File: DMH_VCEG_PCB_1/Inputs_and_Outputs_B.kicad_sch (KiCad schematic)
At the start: 38 parts, among them J11 TS_Jack_6.35mm_Sw, J12 TS_Jack_6.35mm_Sw, J13 TS_Jack_6.35mm_Sw, J14 TS_Jack_6.35mm_Sw, J15 TS_Jack_6.35mm_Sw, J16 TS_Jack_6.35mm_Sw, J17 TS_Jack_6.35mm_Sw, J18 TS_Jack_6.35mm_Sw, J19 TS_Jack_6.35mm_Sw, J20 TS_Jack_6.35mm_Sw, J24 Conn_01x10_PinHeader, J25 Conn_01x10_PinHeader, J26 Conn_01x10_PinHeader, J27 Conn_01x06_PinHeader, U18 TL074, U21 TL074

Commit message: Copied circuit A to B
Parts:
- added R15: 1k, Resistor_THT:R_Axial_DIN0207_L6.3mm_D2.5mm_P7.62mm_Horizontal, symbol Device:R_US
- added R22: 68K, Resistor_THT:R_Axial_DIN0207_L6.3mm_D2.5mm_P7.62mm_Horizontal, symbol Device:R_US
- added R24: 100k, Resistor_THT:R_Axial_DIN0207_L6.3mm_D2.5mm_P7.62mm_Horizontal, symbol Device:R_US
- added U18: TL074, Package_DIP:DIP-14_W7.62mm_Socket, symbol Amplifier_Operational:TL074
- renumbered J24 to J22, R114 to R16, R78 to R17, R73 to R18, R74 to R19, R75 to R20, R76 to R21, R148 to R23, R77 to R25, R56 to R26, R147 to R27, R79 to R28, RV23 to RV12, RV24 to RV13, RV25 to RV14, RV26 to RV15, RV51 to RV16, RV27 to RV17, RV28 to RV18, RV29 to RV19, RV30 to RV20, RV50 to RV21, RV49 to RV22, U21 to U11, U18 to U22
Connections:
- net GND: now also U18.10 (+)
- net SG Out B: now also R24.1; no longer J17.T
- new net: R22.1, R24.2, U18.9 (-)
- new net: R15.2, R22.2, U18.8
- new net: J17.T, R15.1

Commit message: Divided components between PCB 1 and 2
Still need to:
- Place interface pins where needed
- Set "exclude from board" options where needed
- Copy schematic over to PCB 2 project
- Invert "exclude from board" options where needed
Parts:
- removed J27: Conn_01x06_PinHeader, symbol SynthStuff:Conn_01x06_PinHeader
- renumbered J22 to J?, U11 to U17
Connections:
- net GND: now also U18.12 (+); no longer U18.10 (+)
- net at R22.1, R24.2: now also U18.13 (-); no longer U18.9 (-)
- net at R15.2, R22.2: now also U18.14; no longer U18.8
- net at R17.1, RV16.1: now also U17.5 (+); no longer U17.12 (+)
- net at R27.1, RV21.1: now also U17.3 (+); no longer U17.10 (+)
- net at R25.1, R26.1, RV22.1: now also U17.1; no longer U17.8
- net at R28.2, RV22.2, RV22.3: now also U17.2 (-); no longer U17.9 (-)
- net at R23.1, R26.2: now also U17.6 (-); no longer U17.13 (-)
- net at R16.1, R23.2: now also U17.7; no longer U17.14

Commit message: Re-annotated whole circuit
Now need to place interface pins and determine in and out of board settings
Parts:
- gave numbers to parts that had none: 3
- renumbered J24 to J25, J25 to J26, R18 to R181, R19 to R182, R20 to R183, R21 to R184, R22 to R185, R24 to R186, R15 to R187, R25 to R188, R23 to R189, R28 to R190, R26 to R191, R16 to R192, R27 to R193, R17 to R194, RV17 to RV32, RV12 to RV33, RV18 to RV34, RV13 to RV35, RV19 to RV36, RV14 to RV37, RV20 to RV38, RV15 to RV39, RV22 to RV40, RV21 to RV41, RV16 to RV42, U22 to U23

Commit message: Ready for breadboarding
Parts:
- removed unit 1 of J24
- removed unit 2 of J25
- added J24: Conn_01x06_PinHeader, Connector_PinHeader_2.54mm:PinHeader_1x06_P2.54mm_Vertical, symbol SynthStuff:Conn_01x06_PinHeader
- added unit 10 of J25
- added unit 3 of J26
- added unit 2 of J27
- added unit 1 of J27
- RV40, RV41, RV42: footprint Potentiometer_THT:Potentiometer_Bourns_3296X_Horizontal -> Potentiometer_THT:Potentiometer_Bourns_3296W_Vertical
- U17: footprint (none) -> Package_DIP:DIP-14_W7.62mm_Socket
- renumbered J24 to J27, J22 to J27, J23 to J27
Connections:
- net +12V: now also J25.1 (Pin_1)
- net -12V: now also J27.2 (Pin_2); no longer J25.1 (Pin_1)
- net GND: now also J24.6 (Pin_6), J25.10 (Pin_10), J27.1 (Pin_1); no longer J26.2 (Pin_2)
- net SG Out B: now also J26.2 (Pin_2)
- net at J17.T, R187.1: now also J26.3 (Pin_3)

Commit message: PCB 2 placement in progress
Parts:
- RV32: Function Att CV B Zero Adj -> Att CV B Zero
- RV34: Function Dec CV B Zero Adj -> Dec CV B Zero
- RV36: Function Sus CV B Zero Adj -> Sus CV B Zero
- RV38: Function Rel CV B Zero Adj -> Rel CV B Zero
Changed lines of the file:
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@@
 			)
 		)
-		(property "Function" "Sus CV B Zero Adj"
+		(property "Function" "Sus CV B Zero"
 			(at 127 86.868 90)
 			(effects
@@
 			)
 		)
-		(property "Function" "Dec CV B Zero Adj"
+		(property "Function" "Dec CV B Zero"
 			(at 127 55.118 90)
 			(effects
@@
 			)
 		)
-		(property "Function" "Rel CV B Zero Adj"
+		(property "Function" "Rel CV B Zero"
 			(at 127 118.618 90)
 			(effects
@@
 			)
 		)
-		(property "Function" "Att CV B Zero Adj"
+		(property "Function" "Att CV B Zero"
 			(at 127 23.368 90)
 			(effects

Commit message: Synced changes to Circuit B
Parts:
- added R11: 100k, Resistor_THT:R_Axial_DIN0207_L6.3mm_D2.5mm_P7.62mm_Horizontal, symbol Device:R_US
- added R18: 68k, Resistor_THT:R_Axial_DIN0207_L6.3mm_D2.5mm_P7.62mm_Horizontal, symbol Device:R_US
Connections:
- net +12V: now also R18.1
- net GND: now also R11.2; no longer U18.12 (+)
- new net: R11.1, R18.2, U18.12 (+)
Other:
- moved on the sheet: R185, R187, U18D

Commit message: PCB 2 routing in progress
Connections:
- net Att CV B: no longer J27.3 (Pin_3)
- net Dec CV B: no longer J27.6 (Pin_6)
- net Rel CV B: no longer J27.10 (Pin_10)
- net Sus CV B: no longer J27.7 (Pin_7)
- no-connect marks 0 -> 4
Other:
- moved on the sheet: J27C, J27F, J27G, J27J
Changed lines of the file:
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@@
 	)
 	(junction
-		(at 144.78 129.54)
-		(diameter 0)
-		(color 0 0 0 0)
-	)
-	(junction
 		(at 176.53 215.9)
 		(diameter 0)
@@
 	)
 	(junction
-		(at 144.78 66.04)
-		(diameter 0)
-		(color 0 0 0 0)
-	)
-	(junction
-		(at 144.78 34.29)
-		(diameter 0)
-		(color 0 0 0 0)
-	)
-	(junction
 		(at 115.57 63.5)
 		(diameter 0)
@@
 	)
 	(junction
-		(at 144.78 97.79)
-		(diameter 0)
-		(color 0 0 0 0)
-	)
-	(junction
 		(at 138.43 85.09)
 		(diameter 0)
@@
 		(color 0 0 0 0)
 	)
+	(no_connect
+		(at 144.78 63.5)
+	)
+	(no_connect
+		(at 144.78 127)
+	)
+	(no_connect
+		(at 144.78 95.25)
+	)
+	(no_connect
+		(at 144.78 31.75)
+	)
 	(wire
 		(pts
@@
 	(wire
 		(pts
-			(xy 144.78 97.79) (xy 158.75 97.79)
+			(xy 138.43 97.79) (xy 158.75 97.79)
 		)
 		(stroke
@@
 	(wire
 		(pts
-			(xy 144.78 66.04) (xy 158.75 66.04)
+			(xy 138.43 66.04) (xy 158.75 66.04)
 		)
 		(stroke
@@
 	(wire
 		(pts
-			(xy 138.43 66.04) (xy 144.78 66.04)
-		)
-		(stroke
-			(width 0)
-			(type default)
-		)
-	)
-	(wire
-		(pts
 			(xy 105.41 231.14) (xy 109.22 231.14)
 		)
@@
 	(wire
 		(pts
-			(xy 138.43 97.79) (xy 144.78 97.79)
-		)
-		(stroke
-			(width 0)
-			(type default)
-		)
-	)
-	(wire
-		(pts
 			(xy 38.1 149.86) (xy 38.1 175.26)
 		)
@@
 	(wire
 		(pts
-			(xy 144.78 129.54) (xy 158.75 129.54)
-		)
-		(stroke
-			(width 0)
-			(type default)
-		)
-	)
-	(wire
-		(pts
 			(xy 123.19 180.34) (xy 125.73 180.34)
 		)
@@
 	(wire
 		(pts
-			(xy 144.78 34.29) (xy 158.75 34.29)
+			(xy 138.43 34.29) (xy 158.75 34.29)
 		)
 		(stroke
@@
 	(wire
 		(pts
-			(xy 138.43 34.29) (xy 144.78 34.29)
-		)
-		(stroke
-			(width 0)
-			(type default)
-		)
-	)
-	(wire
-		(pts
 			(xy 44.45 228.6) (xy 30.48 228.6)
 		)
@@
 	(wire
 		(pts
-			(xy 138.43 129.54) (xy 144.78 129.54)
+			(xy 138.43 129.54) (xy 158.75 129.54)
 		)
 		(stroke
@@
 	(symbol
 		(lib_id "SynthStuff:Conn_01x10_PinHeader")
-		(at 144.78 124.46 270)
+		(at 144.78 121.92 270)
 		(unit 10)
 		(exclude_from_sim no)
@@
 		(fields_autoplaced yes)
 		(property "Reference" "J27"
-			(at 146.05 125.0949 90)
+			(at 146.05 122.5549 90)
 			(effects
 				(font
@@
 		)
 		(property "Value" "Conn_01x10_PinHeader"
-			(at 142.24 124.46 0)
+			(at 142.24 121.92 0)
 			(effects
 				(font
@@
 		)
 		(property "Footprint" "Connector_PinHeader_2.54mm:PinHeader_1x10_P2.54mm_Vertical"
-			(at 144.78 124.46 0)
+			(at 144.78 121.92 0)
 			(effects
 				(font
@@
 		)
 		(property "Datasheet" "~"
-			(at 144.78 124.46 0)
+			(at 144.78 121.92 0)
 			(effects
 				(font
@@
 		)
 		(property "Description" "Generic connector, single row, 01x10"
-			(at 144.78 124.46 0)
+			(at 144.78 121.92 0)
 			(effects
 				(font
@@
 	(symbol
 		(lib_id "SynthStuff:Conn_01x10_PinHeader")
-		(at 144.78 92.71 270)
+		(at 144.78 90.17 270)
 		(unit 7)
 		(exclude_from_sim no)
@@
 		(fields_autoplaced yes)
 		(property "Reference" "J27"
-			(at 146.05 93.3449 90)
+			(at 146.05 90.8049 90)
 			(effects
 				(font
@@
 		)
 		(property "Value" "Conn_01x10_PinHeader"
-			(at 142.24 92.71 0)
+			(at 142.24 90.17 0)
 			(effects
 				(font
@@
 		)
 		(property "Footprint" "Connector_PinHeader_2.54mm:PinHeader_1x10_P2.54mm_Vertical"
-			(at 144.78 92.71 0)
+			(at 144.78 90.17 0)
 			(effects
 				(font
@@
 		)
 		(property "Datasheet" "~"
-			(at 144.78 92.71 0)
+			(at 144.78 90.17 0)
 			(effects
 				(font
@@
 		)
 		(property "Description" "Generic connector, single row, 01x10"
-			(at 144.78 92.71 0)
+			(at 144.78 90.17 0)
 			(effects
 				(font
@@
 	(symbol
 		(lib_id "SynthStuff:Conn_01x10_PinHeader")
-		(at 144.78 29.21 270)
+		(at 144.78 26.67 270)
 		(unit 3)
 		(exclude_from_sim no)
@@
 		(fields_autoplaced yes)
 		(property "Reference" "J27"
-			(at 146.05 29.8449 90)
+			(at 146.05 27.3049 90)
 			(effects
 				(font
@@
 		)
 		(property "Value" "Conn_01x10_PinHeader"
-			(at 142.24 29.21 0)
+			(at 142.24 26.67 0)
 			(effects
 				(font
@@
 		)
 		(property "Footprint" "Connector_PinHeader_2.54mm:PinHeader_1x10_P2.54mm_Vertical"
-			(at 144.78 29.21 0)
+			(at 144.78 26.67 0)
 			(effects
 				(font
@@
 		)
 		(property "Datasheet" "~"
-			(at 144.78 29.21 0)
+			(at 144.78 26.67 0)
 			(effects
 				(font
@@
 		)
 		(property "Description" "Generic connector, single row, 01x10"
-			(at 144.78 29.21 0)
+			(at 144.78 26.67 0)
 			(effects
 				(font
@@
 	(symbol
 		(lib_id "SynthStuff:Conn_01x10_PinHeader")
-		(at 144.78 60.96 270)
+		(at 144.78 58.42 270)
 		(unit 6)
 		(exclude_from_sim no)
@@
 		(fields_autoplaced yes)
 		(property "Reference" "J27"
-			(at 146.05 61.5949 90)
+			(at 146.05 59.0549 90)
 			(effects
 				(font
@@
 		)
 		(property "Value" "Conn_01x10_PinHeader"
-			(at 142.24 60.96 0)
+			(at 142.24 58.42 0)
 			(effects
 				(font
@@
 		)
 		(property "Footprint" "Connector_PinHeader_2.54mm:PinHeader_1x10_P2.54mm_Vertical"
-			(at 144.78 60.96 0)
+			(at 144.78 58.42 0)
 			(effects
 				(font
@@
 		)
 		(property "Datasheet" "~"
-			(at 144.78 60.96 0)
+			(at 144.78 58.42 0)
 			(effects
 				(font
@@
 		)
 		(property "Description" "Generic connector, single row, 01x10"
-			(at 144.78 60.96 0)
+			(at 144.78 58.42 0)
 			(effects
 				(font

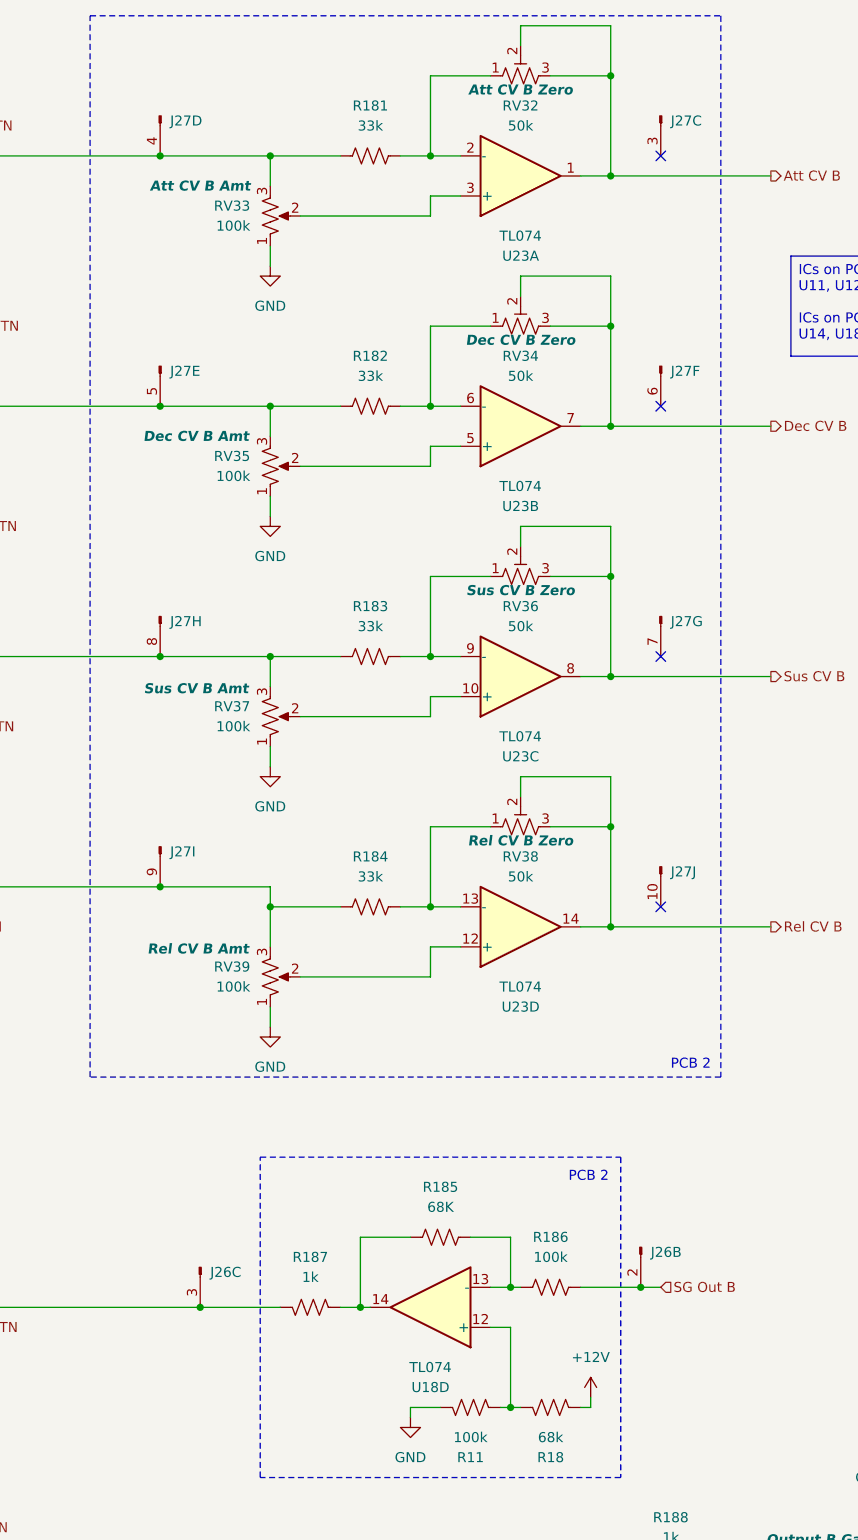
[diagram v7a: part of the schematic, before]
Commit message: Synced PCB 2 schematic to PCB 1
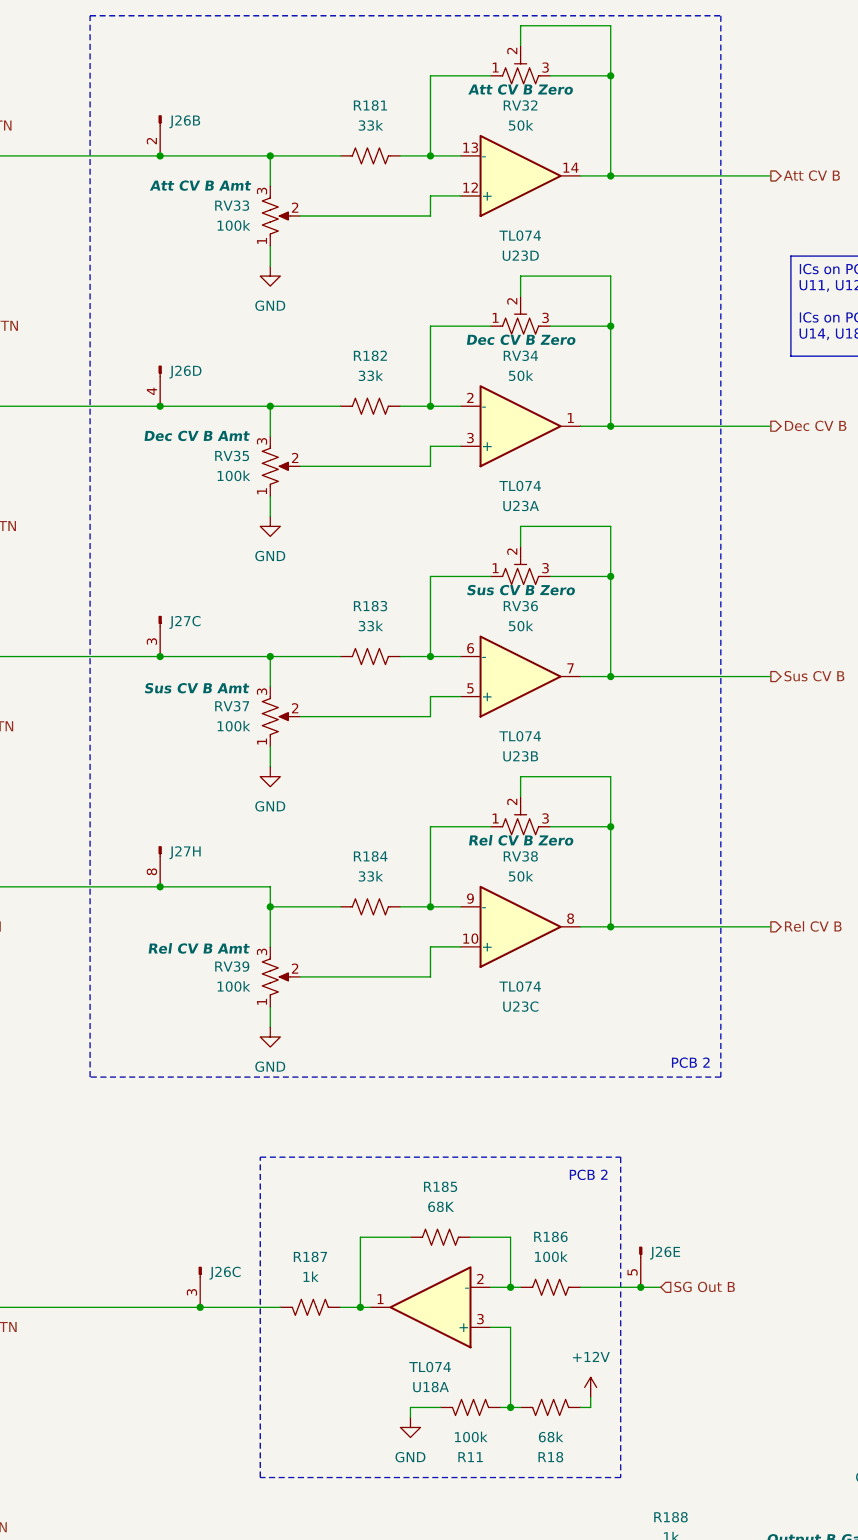
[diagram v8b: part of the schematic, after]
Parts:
- removed unit 10 of J27
- removed unit 7 of J27
- removed unit 3 of J27
- removed unit 6 of J27
- renumbered J27 to J26
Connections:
- net Att CV B: now also U23.14; no longer U23.1
- net Dec CV B: now also U23.1; no longer U23.7
- net Rel CV B: now also U23.8; no longer U23.14
- net SG Out B: now also J26.5 (Pin_5); no longer J26.2 (Pin_2)
- net Sus CV B: now also U23.7; no longer U23.8
- net at R11.1, R18.2: now also U18.3 (+); no longer U18.12 (+)
- net at R183.2, RV36.1: now also U23.6 (-); no longer U23.9 (-)
- net at J14.T, R184.1, RV39.3: now also J27.8 (Pin_8); no longer J27.9 (Pin_9)
- net at J11.T, R181.1, RV33.3: now also J26.2 (Pin_2); no longer J26.4 (Pin_4)
- net at R185.1, R186.2: now also U18.2 (-); no longer U18.13 (-)
- net at R185.2, R187.2: now also U18.1; no longer U18.14
- net at J12.T, R182.1, RV35.3: now also J26.4 (Pin_4); no longer J26.5 (Pin_5)
- net at R182.2, RV34.1: now also U23.2 (-); no longer U23.6 (-)
- net at R181.2, RV32.1: now also U23.13 (-); no longer U23.2 (-)
- net at RV33.2: now also U23.12 (+); no longer U23.3 (+)
- net at RV35.2: now also U23.3 (+); no longer U23.5 (+)
- net at R184.2, RV38.1: now also U23.9 (-); no longer U23.13 (-)
- net at J13.T, R183.1, RV37.3: now also J27.3 (Pin_3); no longer J27.8 (Pin_8)
- net at RV39.2: now also U23.10 (+); no longer U23.12 (+)
- net at RV37.2: now also U23.5 (+); no longer U23.10 (+)
- no-connect marks 4 -> 0
